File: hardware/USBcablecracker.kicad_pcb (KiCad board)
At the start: 2 copper layers, 100 x 50 mm, 54 parts, among them P1 USB_A, P10 USB_A, P11 USB_B, P2 CONN_01X02, P3 USB_B-Micro, P7 USB_B-Mini, P8 USB_B-Micro-3.0, P9 USB_TYPEC-S, SW1 Switch_SPDT_x2, U2 LMV358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

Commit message: fixes accidental deletion of U1
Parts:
- added U1: ATmega32U4-AU, Housings_QFP:TQFP-44_10x10mm_Pitch0.8mm, B.Cu at (127.2, 72.3)
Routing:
- net (no net): track 6.71 -> 0.00 mm, vias 1 -> 0
- net +5V: track 219.7 -> 224.8 mm
- net GND: track 1.20 -> 2.76 mm, vias 0 -> 1
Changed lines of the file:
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@@
 (kicad_pcb (version 4) (host pcbnew 4.0.7+dfsg1-1)
   (general
-    (links 106)
+    (links 138)
     (no_connects 0)
     (area 47.6808 47.625 150.075001 102.075)
@@
     (tracks 834)
     (zones 0)
-    (modules 54)
-    (nets 89)
+    (modules 55)
+    (nets 101)
   )
   (page A4)
@@
   (net 87 "Net-(C13-Pad1)")
   (net 88 +5V)
+  (net 89 /A5)
+  (net 90 /A4)
+  (net 91 /A3)
+  (net 92 /A2)
+  (net 93 /A1)
+  (net 94 /IO10)
+  (net 95 /IO9)
+  (net 96 /D3)
+  (net 97 /D2)
+  (net 98 /D1)
+  (net 99 /D0)
+  (net 100 /IO8)
   (net_class Default "This is the default net class."
     (clearance 0.2)
@@
     (uvia_drill 0.1)
     (add_net /A0)
+    (add_net /A1)
+    (add_net /A2)
+    (add_net /A3)
+    (add_net /A4)
+    (add_net /A5)
     (add_net /AREF)
     (add_net /D+)
     (add_net /D-)
+    (add_net /D0)
+    (add_net /D1)
+    (add_net /D2)
+    (add_net /D3)
     (add_net /D4)
     (add_net /D5)
@@
     (add_net /DIN-)
     (add_net /HWB)
+    (add_net /IO10)
     (add_net /IO11)
     (add_net /IO12)
     (add_net /IO13)
+    (add_net /IO8)
+    (add_net /IO9)
     (add_net /MISO)
     (add_net /MOSI)
@@
     )
   )
+  (module Housings_QFP:TQFP-44_10x10mm_Pitch0.8mm (layer B.Cu)
+    (at 127.216 72.314)
+    (descr "44-Lead Plastic Thin Quad Flatpack (PT) - 10x10x1.0 mm Body [TQFP] (see Microchip Packaging Specification 00000049BS.pdf)")
+    (tags "QFP 0.8")
+    (attr smd)
+    (fp_text reference U1 (at 0 7.45) (layer B.SilkS)
+      (effects (font (size 1 1) (thickness 0.15)) (justify mirror))
+    )
+    (fp_text value ATmega32U4-AU (at 0 -7.45) (layer B.Fab)
+      (effects (font (size 1 1) (thickness 0.15)) (justify mirror))
+    )
+    (fp_text user %R (at 0 0) (layer B.Fab) hide
+      (effects (font (size 1 1) (thickness 0.15)) (justify mirror))
+    )
+    (fp_line (start -4 5) (end 5 5) (layer B.Fab) (width 0.15))
+    (fp_line (start 5 5) (end 5 -5) (layer B.Fab) (width 0.15))
+    (fp_line (start 5 -5) (end -5 -5) (layer B.Fab) (width 0.15))
+    (fp_line (start -5 -5) (end -5 4) (layer B.Fab) (width 0.15))
+    (fp_line (start -5 4) (end -4 5) (layer B.Fab) (width 0.15))
+    (fp_line (start -6.7 6.7) (end -6.7 -6.7) (layer B.CrtYd) (width 0.05))
+    (fp_line (start 6.7 6.7) (end 6.7 -6.7) (layer B.CrtYd) (width 0.05))
+    (fp_line (start -6.7 6.7) (end 6.7 6.7) (layer B.CrtYd) (width 0.05))
+    (fp_line (start -6.7 -6.7) (end 6.7 -6.7) (layer B.CrtYd) (width 0.05))
+    (fp_line (start -5.175 5.175) (end -5.175 4.6) (layer B.SilkS) (width 0.15))
+    (fp_line (start 5.175 5.175) (end 5.175 4.5) (layer B.SilkS) (width 0.15))
+    (fp_line (start 5.175 -5.175) (end 5.175 -4.5) (layer B.SilkS) (width 0.15))
+    (fp_line (start -5.175 -5.175) (end -5.175 -4.5) (layer B.SilkS) (width 0.15))
+    (fp_line (start -5.175 5.175) (end -4.5 5.175) (layer B.SilkS) (width 0.15))
+    (fp_line (start -5.175 -5.175) (end -4.5 -5.175) (layer B.SilkS) (width 0.15))
+    (fp_line (start 5.175 -5.175) (end 4.5 -5.175) (layer B.SilkS) (width 0.15))
+    (fp_line (start 5.175 5.175) (end 4.5 5.175) (layer B.SilkS) (width 0.15))
+    (fp_line (start -5.175 4.6) (end -6.45 4.6) (layer B.SilkS) (width 0.15))
+    (pad 1 smd rect (at -5.7 4) (size 1.5 0.55) (layers B.Cu B.Paste B.Mask)
+      (net 35 /D7))
+    (pad 2 smd rect (at -5.7 3.2) (size 1.5 0.55) (layers B.Cu B.Paste B.Mask)
+      (net 88 +5V))
+    (pad 3 smd rect (at -5.7 2.4) (size 1.5 0.55) (layers B.Cu B.Paste B.Mask)
+      (net 43 /D-))
+    (pad 4 smd rect (at -5.7 1.6) (size 1.5 0.55) (layers B.Cu B.Paste B.Mask)
+      (net 42 /D+))
+    (pad 5 smd rect (at -5.7 0.8) (size 1.5 0.55) (layers B.Cu B.Paste B.Mask)
+      (net 1 GND))
+    (pad 6 smd rect (at -5.7 0) (size 1.5 0.55) (layers B.Cu B.Paste B.Mask)
+      (net 49 "Net-(C7-Pad2)"))
+    (pad 7 smd rect (at -5.7 -0.8) (size 1.5 0.55) (layers B.Cu B.Paste B.Mask)
+      (net 88 +5V))
+    (pad 8 smd rect (at -5.7 -1.6) (size 1.5 0.55) (layers B.Cu B.Paste B.Mask)
+      (net 39 /RX_LED))
+    (pad 9 smd rect (at -5.7 -2.4) (size 1.5 0.55) (layers B.Cu B.Paste B.Mask)
+      (net 26 /SCK))
+    (pad 10 smd rect (at -5.7 -3.2) (size 1.5 0.55) (layers B.Cu B.Paste B.Mask)
+      (net 27 /MOSI))
+    (pad 11 smd rect (at -5.7 -4) (size 1.5 0.55) (layers B.Cu B.Paste B.Mask)
+      (net 25 /MISO))
+    (pad 12 smd rect (at -4 -5.7 270) (size 1.5 0.55) (layers B.Cu B.Paste B.Mask)
+      (net 36 /IO11))
+    (pad 13 smd rect (at -3.2 -5.7 270) (size 1.5 0.55) (layers B.Cu B.Paste B.Mask)
+      (net 28 /RESET))
+    (pad 14 smd rect (at -2.4 -5.7 270) (size 1.5 0.55) (layers B.Cu B.Paste B.Mask)
+      (net 88 +5V))
+    (pad 15 smd rect (at -1.6 -5.7 270) (size 1.5 0.55) (layers B.Cu B.Paste B.Mask)
+      (net 1 GND))
+    (pad 16 smd rect (at -0.8 -5.7 270) (size 1.5 0.55) (layers B.Cu B.Paste B.Mask)
+      (net 82 /X-))
+    (pad 17 smd rect (at 0 -5.7 270) (size 1.5 0.55) (layers B.Cu B.Paste B.Mask)
+      (net 81 /X+))
+    (pad 18 smd rect (at 0.8 -5.7 270) (size 1.5 0.55) (layers B.Cu B.Paste B.Mask)
+      (net 96 /D3))
+    (pad 19 smd rect (at 1.6 -5.7 270) (size 1.5 0.55) (layers B.Cu B.Paste B.Mask)
+      (net 97 /D2))
+    (pad 20 smd rect (at 2.4 -5.7 270) (size 1.5 0.55) (layers B.Cu B.Paste B.Mask)
+      (net 99 /D0))
+    (pad 21 smd rect (at 3.2 -5.7 270) (size 1.5 0.55) (layers B.Cu B.Paste B.Mask)
+      (net 98 /D1))
+    (pad 22 smd rect (at 4 -5.7 270) (size 1.5 0.55) (layers B.Cu B.Paste B.Mask)
+      (net 40 /TX_LED))
+    (pad 23 smd rect (at 5.7 -4) (size 1.5 0.55) (layers B.Cu B.Paste B.Mask)
+      (net 1 GND))
+    (pad 24 smd rect (at 5.7 -3.2) (size 1.5 0.55) (layers B.Cu B.Paste B.Mask)
+      (net 88 +5V))
+    (pad 25 smd rect (at 5.7 -2.4) (size 1.5 0.55) (layers B.Cu B.Paste B.Mask)
+      (net 32 /D4))
+    (pad 26 smd rect (at 5.7 -1.6) (size 1.5 0.55) (layers B.Cu B.Paste B.Mask)
+      (net 37 /IO12))
+    (pad 27 smd rect (at 5.7 -0.8) (size 1.5 0.55) (layers B.Cu B.Paste B.Mask)
+      (net 34 /D6))
+    (pad 28 smd rect (at 5.7 0) (size 1.5 0.55) (layers B.Cu B.Paste B.Mask)
+      (net 100 /IO8))
+    (pad 29 smd rect (at 5.7 0.8) (size 1.5 0.55) (layers B.Cu B.Paste B.Mask)
+      (net 95 /IO9))
+    (pad 30 smd rect (at 5.7 1.6) (size 1.5 0.55) (layers B.Cu B.Paste B.Mask)
+      (net 94 /IO10))
+    (pad 31 smd rect (at 5.7 2.4) (size 1.5 0.55) (layers B.Cu B.Paste B.Mask)
+      (net 33 /D5))
+    (pad 32 smd rect (at 5.7 3.2) (size 1.5 0.55) (layers B.Cu B.Paste B.Mask)
+      (net 38 /IO13))
+    (pad 33 smd rect (at 5.7 4) (size 1.5 0.55) (layers B.Cu B.Paste B.Mask)
+      (net 41 /HWB))
+    (pad 34 smd rect (at 4 5.7 270) (size 1.5 0.55) (layers B.Cu B.Paste B.Mask)
+      (net 88 +5V))
+    (pad 35 smd rect (at 3.2 5.7 270) (size 1.5 0.55) (layers B.Cu B.Paste B.Mask)
+      (net 1 GND))
+    (pad 36 smd rect (at 2.4 5.7 270) (size 1.5 0.55) (layers B.Cu B.Paste B.Mask)
+      (net 46 /A0))
+    (pad 37 smd rect (at 1.6 5.7 270) (size 1.5 0.55) (layers B.Cu B.Paste B.Mask)
+      (net 93 /A1))
+    (pad 38 smd rect (at 0.8 5.7 270) (size 1.5 0.55) (layers B.Cu B.Paste B.Mask)
+      (net 92 /A2))
+    (pad 39 smd rect (at 0 5.7 270) (size 1.5 0.55) (layers B.Cu B.Paste B.Mask)
+      (net 91 /A3))
+    (pad 40 smd rect (at -0.8 5.7 270) (size 1.5 0.55) (layers B.Cu B.Paste B.Mask)
+      (net 90 /A4))
+    (pad 41 smd rect (at -1.6 5.7 270) (size 1.5 0.55) (layers B.Cu B.Paste B.Mask)
+      (net 89 /A5))
+    (pad 42 smd rect (at -2.4 5.7 270) (size 1.5 0.55) (layers B.Cu B.Paste B.Mask)
+      (net 24 /AREF))
+    (pad 43 smd rect (at -3.2 5.7 270) (size 1.5 0.55) (layers B.Cu B.Paste B.Mask)
+      (net 1 GND))
+    (pad 44 smd rect (at -4 5.7 270) (size 1.5 0.55) (layers B.Cu B.Paste B.Mask)
+      (net 88 +5V))
+    (model ${KISYS3DMOD}/Housings_QFP.3dshapes/TQFP-44_10x10mm_Pitch0.8mm.wrl
+      (at (xyz 0 0 0))
+      (scale (xyz 1 1 1))
+      (rotate (xyz 0 0 0))
+    )
+  )
   (gr_text USBcablecracker (at 70.5 97.5) (layer B.SilkS)
     (effects (font (size 2 2) (thickness 0.15)) (justify mirror))
@@
   (gr_line (start 150 50) (end 50 50) (angle 90) (layer Edge.Cuts) (width 0.15))
   (gr_line (start 50 100) (end 150 100) (angle 90) (layer Edge.Cuts) (width 0.15))
-  (segment (start 121.5 73.1) (end 120.087642 73.1) (width 0.4) (layer B.Cu) (net 0))
-  (segment (start 120.087642 73.1) (end 119.980237 73.207405) (width 0.4) (layer B.Cu) (net 0))
-  (via (at 119.980237 73.207405) (size 0.6) (drill 0.4) (layers F.Cu B.Cu) (net 0))
-  (segment (start 124.8 69.52) (end 124.8 69.65) (width 0.4) (layer B.Cu) (net 0))
-  (segment (start 124.8 66.6) (end 124.8 69.52) (width 0.4) (layer B.Cu) (net 0))
-  (segment (start 122.39 71.5) (end 123.6 71.5) (width 0.4) (layer B.Cu) (net 0))
-  (segment (start 121.5 71.5) (end 122.39 71.5) (width 0.4) (layer B.Cu) (net 0))
+  (segment (start 121.5 73.1) (end 120.087642 73.1) (width 0.4) (layer B.Cu) (net 1))
+  (segment (start 120.087642 73.1) (end 119.980237 73.207405) (width 0.4) (layer B.Cu) (net 1))
+  (via (at 119.980237 73.207405) (size 0.6) (drill 0.4) (layers F.Cu B.Cu) (net 1))
   (segment (start 115.7009 54.96254) (end 116.9009 54.96254) (width 0.3) (layer F.Cu) (net 1))
   (segment (start 104.525736 87.15) (end 104.95 87.15) (width 0.3) (layer F.Cu) (net 2))
@@
   (segment (start 108.8 84.8) (end 108.9 84.8) (width 0.3) (layer B.Cu) (net 87))
   (segment (start 106.7 82.9) (end 106.9 82.9) (width 0.3) (layer B.Cu) (net 87))
+  (segment (start 124.8 69.52) (end 124.8 69.65) (width 0.4) (layer B.Cu) (net 88))
+  (segment (start 124.8 66.6) (end 124.8 69.52) (width 0.4) (layer B.Cu) (net 88))
+  (segment (start 122.39 71.5) (end 123.6 71.5) (width 0.4) (layer B.Cu) (net 88))
+  (segment (start 121.5 71.5) (end 122.39 71.5) (width 0.4) (layer B.Cu) (net 88))
   (segment (start 149.06 94.158) (end 149.06 90.348) (width 1) (layer F.Cu) (net 88))
   (segment (start 149.06 90.348) (end 149.06 84.633) (width 1) (layer F.Cu) (net 88))

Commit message: proper repo URL
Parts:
- moved DS1 0.29 mm to (73.7, 53.1)
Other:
- board text added: "https://github.com/schwert/USBcablecracker"
- board text removed: "https://github.com/scwhert/USBcablecracker"
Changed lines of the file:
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@@
   )
   (module Display:WC1602A (layer F.Cu)
-    (at 74 53)
+    (at 73.749 53.137)
     (descr http://www.kamami.pl/dl/wc1602a0.pdf)
     (tags "LCD 16x2 Alphanumeric 16pin")
@@
     (effects (font (size 1 1) (thickness 0.15)))
   )
-  (gr_text D13 (at 143 65.5) (layer B.SilkS)
+  (gr_text D13 (at 147.663 65.202) (layer B.SilkS)
     (effects (font (size 1 1) (thickness 0.15)) (justify mirror))
   )
-  (gr_text TX (at 142.4 72.7) (layer B.SilkS)
+  (gr_text TX (at 147.917 72.695) (layer B.SilkS)
     (effects (font (size 1 1) (thickness 0.15)) (justify mirror))
   )
-  (gr_text RX (at 142.6 79.7) (layer B.SilkS)
+  (gr_text RX (at 147.028 89.459) (layer B.SilkS)
     (effects (font (size 1 1) (thickness 0.15)) (justify mirror))
   )
@@
   )
   (gr_line (start 50 100) (end 50 50) (angle 90) (layer Edge.Cuts) (width 0.15))
-  (gr_text https://github.com/scwhert/USBcablecracker (at 128 88.4) (layer F.SilkS)
+  (gr_text https://github.com/schwert/USBcablecracker (at 128 88.4) (layer F.SilkS)
     (effects (font (size 1 1) (thickness 0.15)))
   )

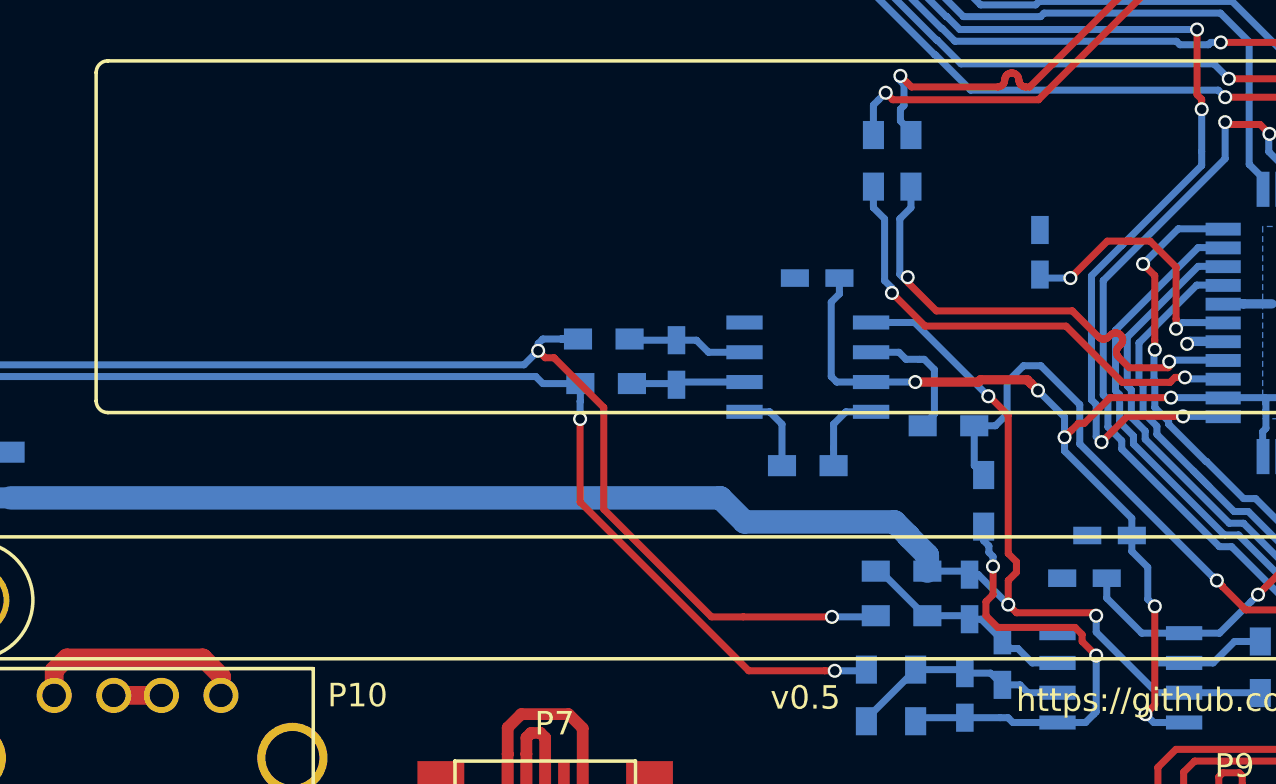
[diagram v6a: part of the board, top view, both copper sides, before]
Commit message: silkscreen prettyness
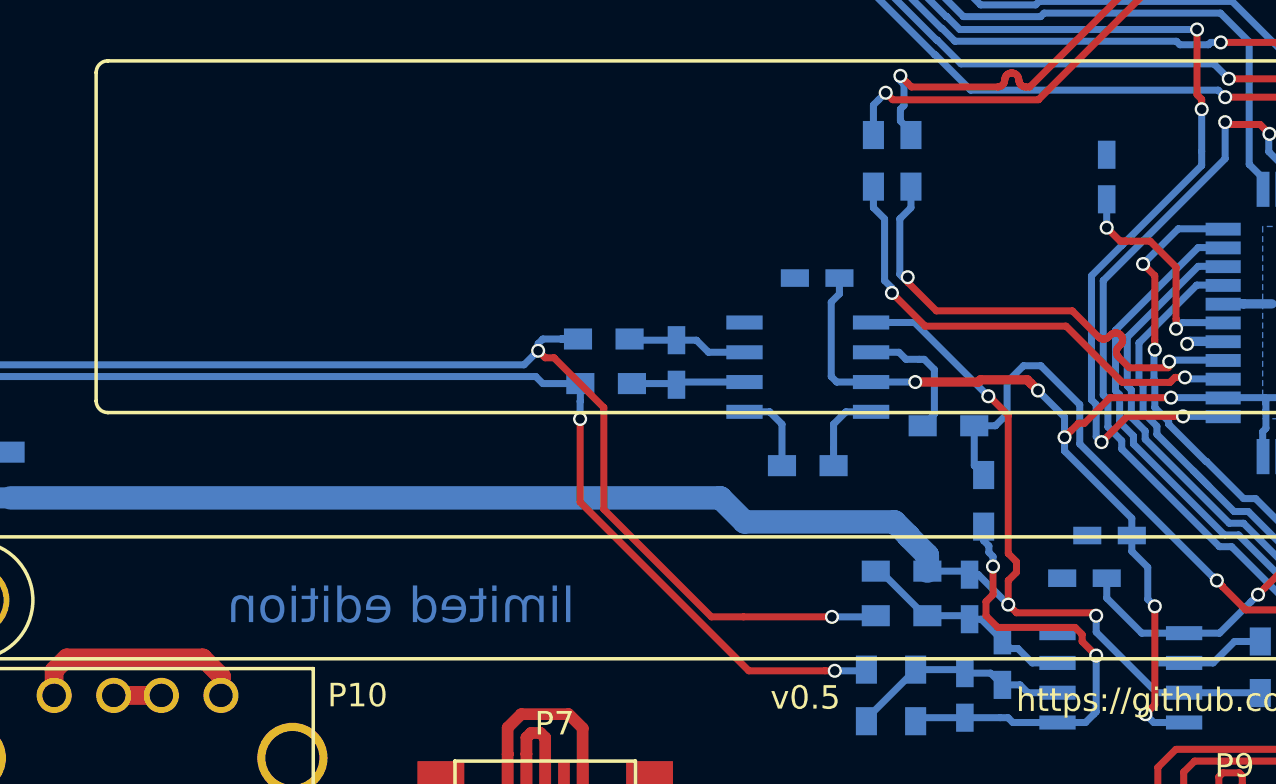
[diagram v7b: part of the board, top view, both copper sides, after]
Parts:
- moved C7 4.29 mm to (116.5, 66.1)
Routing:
- net Net-(C7-Pad2): track 11.9 -> 9.72 mm
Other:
- board text added: "#HTTC2017"
- board text added: "limited edition"
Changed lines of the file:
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@@
     (links 138)
     (no_connects 0)
-    (area 47.6808 47.625 150.075001 102.075)
+    (area 49.924999 49.924999 150.075001 100.075001)
     (thickness 1.6)
-    (drawings 23)
+    (drawings 25)
     (tracks 834)
     (zones 0)
@@
   )
   (module Capacitors_SMD:C_0603_HandSoldering (layer B.Cu)
-    (at 113.7 69.3 270)
+    (at 116.548 66.091 270)
     (descr "Capacitor SMD 0603, hand soldering")
     (tags "capacitor 0603")
@@
     )
   )
+  (gr_text "limited edition" (at 86.449 84.379) (layer B.Cu)
+    (effects (font (size 1.5 1.5) (thickness 0.2)) (justify mirror))
+  )
+  (gr_text "#HTTC2017" (at 85.179 80.696) (layer B.SilkS)
+    (effects (font (size 3 3) (thickness 0.5) italic) (justify mirror))
+  )
   (gr_text USBcablecracker (at 70.5 97.5) (layer B.SilkS)
     (effects (font (size 2 2) (thickness 0.15)) (justify mirror))
@@
   (segment (start 98.2 73.05) (end 96.25 73.05) (width 0.3) (layer B.Cu) (net 48))
   (segment (start 96.25 73.05) (end 96.2 73) (width 0.3) (layer B.Cu) (net 48))
-  (segment (start 115 70.4) (end 113.85 70.4) (width 0.3) (layer B.Cu) (net 49))
-  (segment (start 113.85 70.4) (end 113.7 70.25) (width 0.3) (layer B.Cu) (net 49))
-  (segment (start 116.575 68.825) (end 115 70.4) (width 0.3) (layer F.Cu) (net 49))
-  (via (at 115 70.4) (size 0.6) (drill 0.4) (layers F.Cu B.Cu) (net 49))
+  (segment (start 116.548 68.25) (end 116.548 67.041) (width 0.3) (layer B.Cu) (net 49))
+  (segment (start 117.375 68.825) (end 117.123 68.825) (width 0.3) (layer F.Cu) (net 49))
+  (segment (start 117.123 68.825) (end 116.548 68.25) (width 0.3) (layer F.Cu) (net 49))
+  (via (at 116.548 68.25) (size 0.6) (drill 0.4) (layers F.Cu B.Cu) (net 49))
+  (segment (start 117.375 68.825) (end 117.25 68.825) (width 0.3) (layer F.Cu) (net 49))
   (segment (start 117.6 68.825) (end 117.375 68.825) (width 0.3) (layer F.Cu) (net 49))
   (segment (start 118.4 68.825) (end 117.6 68.825) (width 0.3) (layer F.Cu) (net 49))
-  (segment (start 117.6 68.825) (end 116.575 68.825) (width 0.3) (layer F.Cu) (net 49))
   (segment (start 118.4 68.825) (end 119.506499 69.931499) (width 0.3) (layer F.Cu) (net 49))
   (segment (start 119.506499 72.13849) (end 119.506499 72.562754) (width 0.3) (layer F.Cu) (net 49))
